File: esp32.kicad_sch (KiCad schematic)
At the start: 26 parts, among them J5 TC2030-IDC, J8 USB_C_Receptacle_USB2.0, J9 Conn_01x04, SW1 GT-TC029B-H025-L1N, SW2 GT-TC029B-H025-L1N, U11 RT9080-33GJ5, U12 ESP32-S3-WROOM-1, Y1 32.768kHz

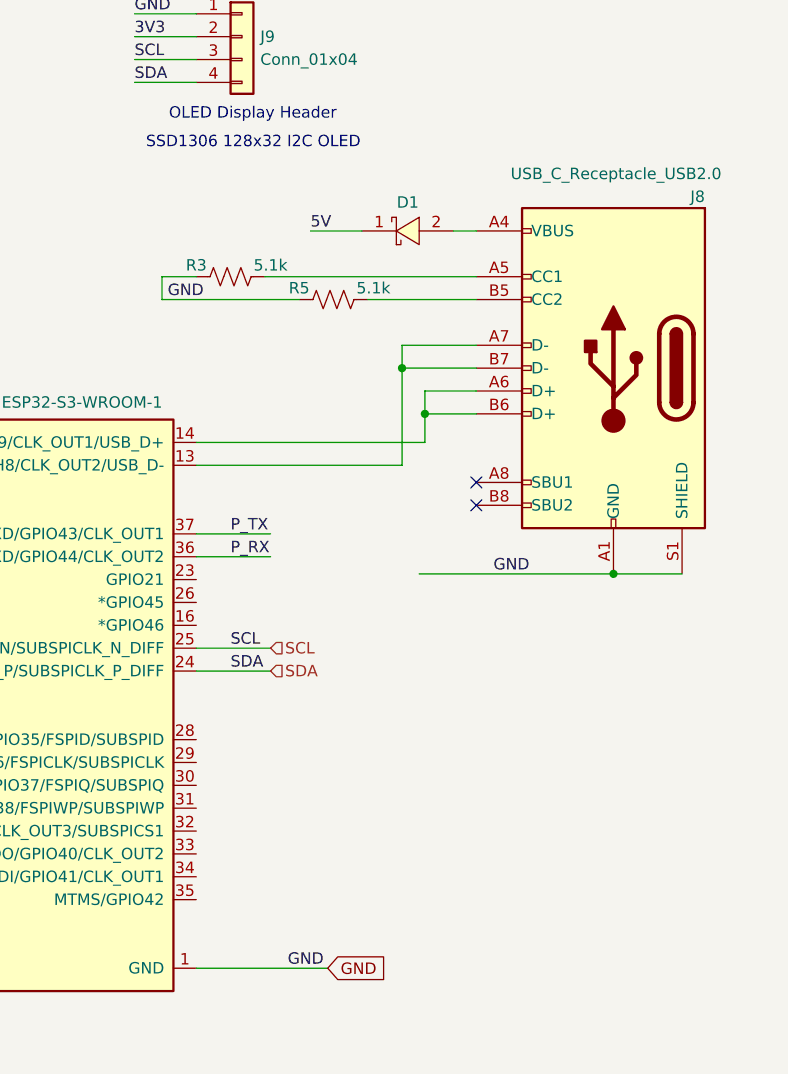
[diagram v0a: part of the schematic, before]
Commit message: Power analysis; updates to 205pd
Started analysis based on the 204 with an architecture diagram and with an smath document. Copied over manually changes from the 205 branch and started updating the schematic with USB PD capabilities. Only added decoy USB PD chip (CH224K), still need to fix power supplies.
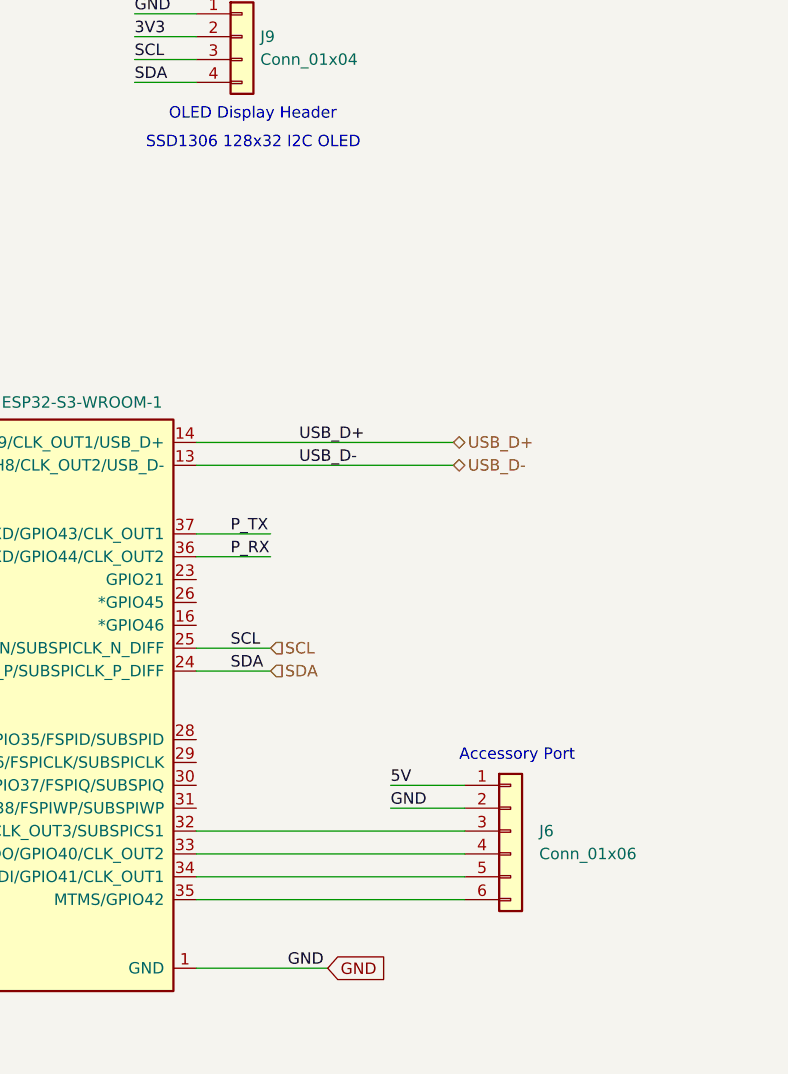
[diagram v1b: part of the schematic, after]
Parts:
- removed D1: SS310, Diode_SMD:D_SMA, symbol lcsc:SS310_C85658
- removed J8: USB_C_Receptacle_USB2.0, Connector_USB:USB_C_Receptacle_GCT_USB4105-xx-A_16P_TopMnt_Horizontal, symbol Connector:USB_C_Receptacle_USB2.0
- removed R3, R5: 5.1k, Resistor_SMD:R_0402_1005Metric, symbol Device:R_US
- added J6: Conn_01x06, Connector_PinHeader_2.54mm:PinHeader_1x06_P2.54mm_Vertical, symbol Connector_Generic:Conn_01x06
- J9: footprint Connector_PinSocket_2.54mm:PinSocket_1x04_P2.54mm_Vertical_SMD_Pin1Right -> bitaxe:PinHeader_1x04_P2.54mm_Vertical_shifted
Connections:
- net 5V: now also J6.1 (Pin_1)
- net GND: now also J6.2 (Pin_2)
- net USB_D+: now reaches U12.14 (GPIO20/U1CTS/ADC2_CH9/CLK_OUT1/USB_D+)
- net USB_D-: now reaches U12.13 (GPIO19/U1RTS/ADC2_CH8/CLK_OUT2/USB_D-)
- net at U12.32 (MTCK/GPIO39/CLK_OUT3/SUBSPICS1): now also J6.3 (Pin_3)
- net at U12.33 (MTDO/GPIO40/CLK_OUT2): now also J6.4 (Pin_4)
- net at U12.34 (MTDI/GPIO41/CLK_OUT1): now also J6.5 (Pin_5)
- net at U12.35 (MTMS/GPIO42): now also J6.6 (Pin_6)
- no-connect marks 2 -> 0
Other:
- note added: "Accessory Port"

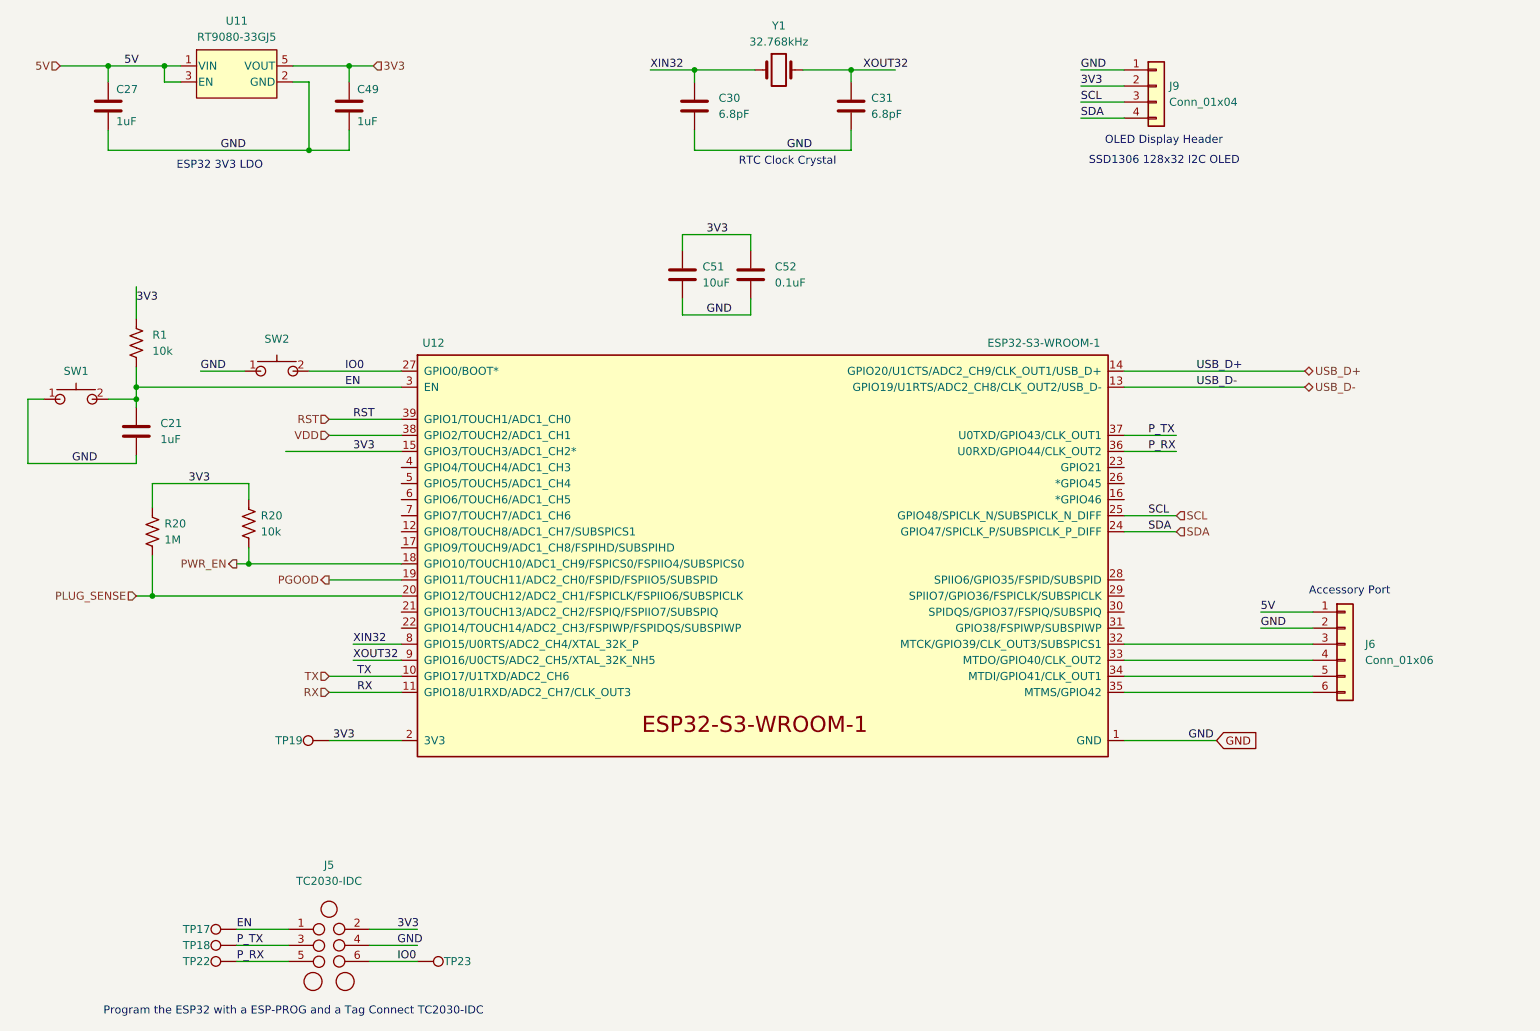
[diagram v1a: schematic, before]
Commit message: Worked on VDD
Started importing SiC431A for VDD supply. Yet to do Vfb, Mode, Pgood, boot, phase, en. Moved power supplies to power page. Configured CH224K to 12V
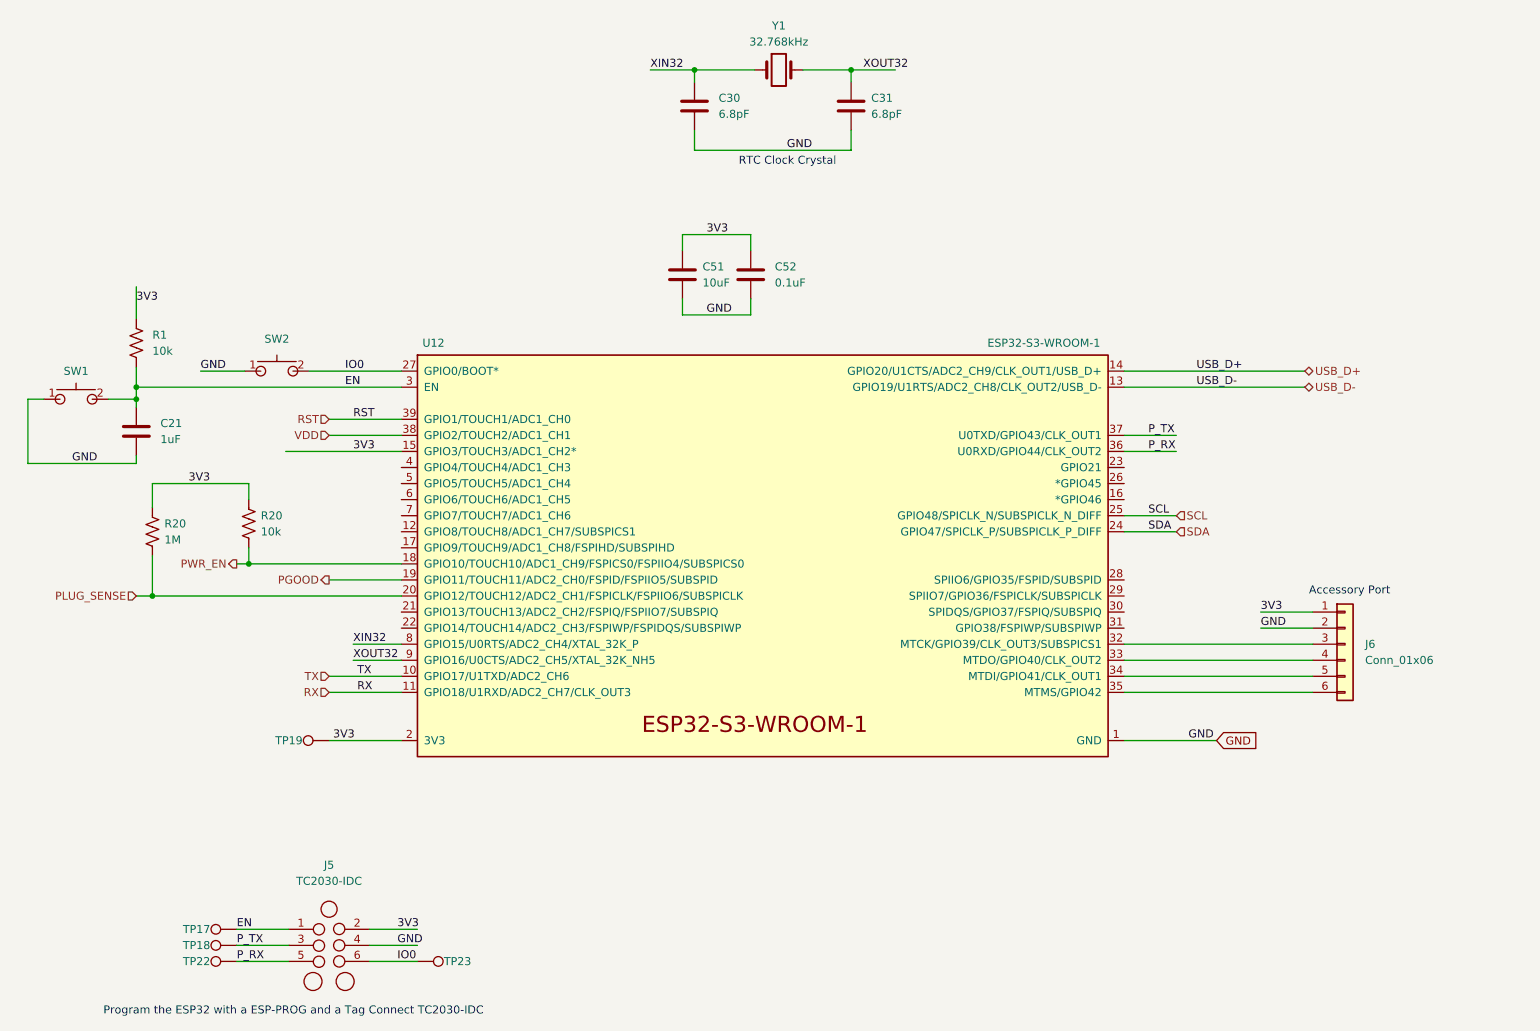
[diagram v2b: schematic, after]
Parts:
- removed C27, C49: 1uF, Capacitor_SMD:C_0402_1005Metric, symbol Device:C
- removed J9: Conn_01x04, bitaxe:PinHeader_1x04_P2.54mm_Vertical_shifted, symbol Connector_Generic:Conn_01x04
- removed U11: RT9080-33GJ5, bitaxe:RT9080-33GJ5, symbol bitaxe:RT9080-33GJ5
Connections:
- net 5V is gone; now on net 3V3: J6.1 (Pin_1)
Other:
- note removed: "ESP32 3V3 LDO"
- note removed: "OLED Display Header"
- note removed: "SSD1306 128x32 I2C OLED"

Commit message: SCH Draft 3, PCB Start
Finished some last minute changes to change 1V8 to 1V2 based on discord feedback. Updated level shifter and moved 25MHz oscillator to use 3V3 and be shifted down. Started working on layout.
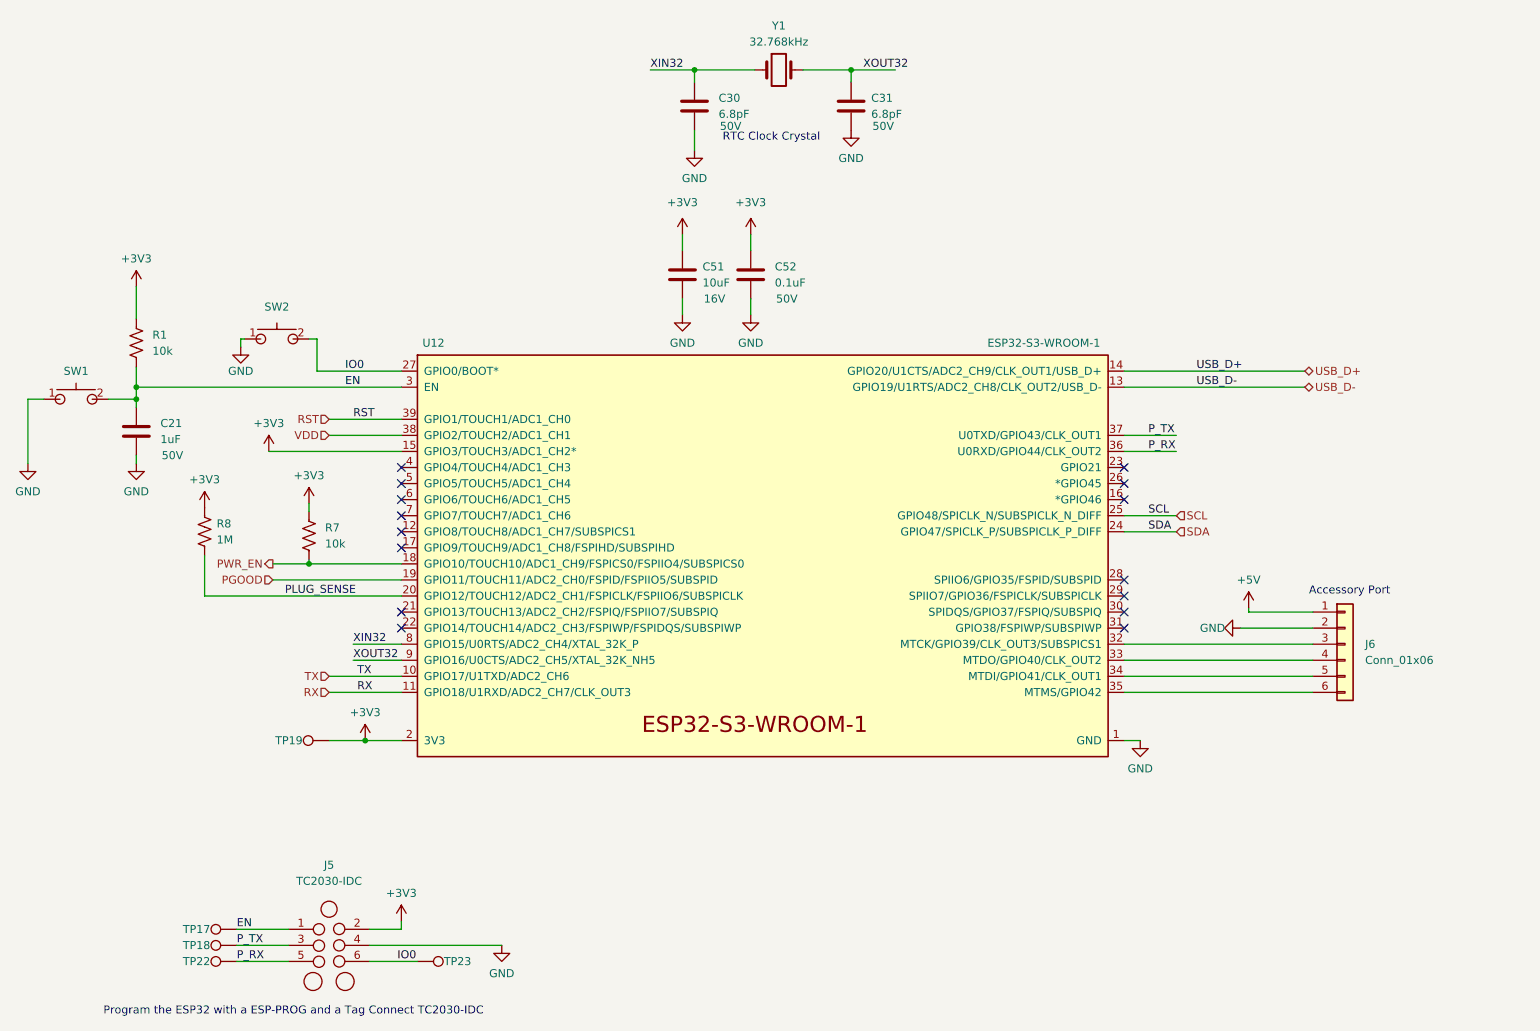
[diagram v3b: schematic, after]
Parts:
- removed R20: 1M, Resistor_SMD:R_0402_1005Metric, symbol Device:R_US
- removed R20: 10k, Resistor_SMD:R_0402_1005Metric, symbol Device:R_US
- added R7: 10k, Resistor_SMD:R_0402_1005Metric, symbol Device:R_US
- added R8: 1M, Resistor_SMD:R_0402_1005Metric, symbol Device:R_US
- C21: footprint Capacitor_SMD:C_0402_1005Metric -> Capacitor_SMD:C_0603_1608Metric; DK 587-5514-1-ND -> 311-2082-1-ND; PARTNO EMK105BJ105MV-F -> CC0603KRX7R9BB105; Voltage (none) -> 50V
- C30, C31: Voltage (none) -> 50V
- C51: Voltage (none) -> 16V
- C52: DK 1292-1639-1-ND -> 490-13342-1-ND; PARTNO 0402X104K100CT -> GRM155R71H104KE14J; Voltage (none) -> 50V
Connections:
- net PLUG_SENSE: now also R8.2
- net PWR_EN: now also R7.2
- net 3V3 renamed +3V3
- net +3V3: now also R7.1, R8.1; no longer J6.1 (Pin_1)
- new net +5V: J6.1 (Pin_1)
- no-connect marks 0 -> 15
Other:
- moved on the sheet: SW2
